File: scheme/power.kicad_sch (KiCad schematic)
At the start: 63 parts, among them J3 Conn_01x01, J4 Conn_01x01, U3 TPS53647, U36 MCP1824T-1202E, U6 AP3211, U7 MCP1824T-0802E

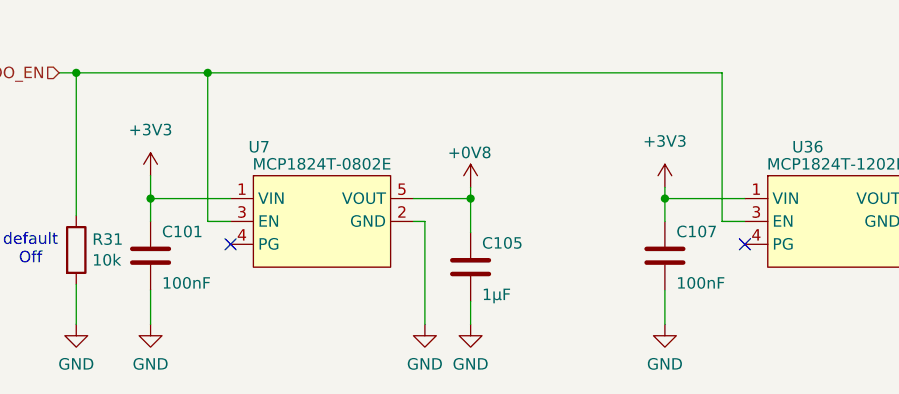
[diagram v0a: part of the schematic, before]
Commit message: Updated schematics with correct cap rating
We upgraded certain capacitors to a higher nF rating and have changed the schematic to reflect it so the BOM can be generated accurately.
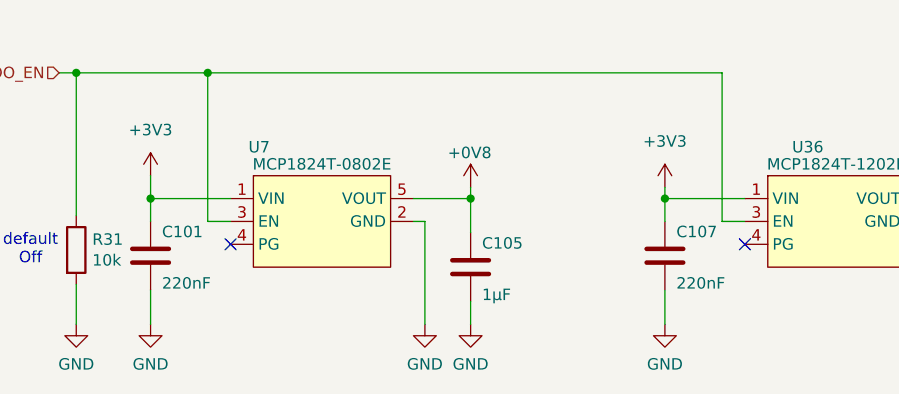
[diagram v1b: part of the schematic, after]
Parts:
- C101, C107: value 100nF -> 220nF
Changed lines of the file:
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@@
 			)
 		)
-		(property "Value" "100nF"
+		(property "Value" "220nF"
 			(at 238.125 266.065 0)
 			(effects
@@
 			)
 		)
-		(property "Value" "100nF"
+		(property "Value" "220nF"
 			(at 180.975 266.065 0)
 			(effects
